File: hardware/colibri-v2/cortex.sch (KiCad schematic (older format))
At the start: 54 parts

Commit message: Work on PWM, USB, MEMS, Power
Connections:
- wire segments 444 -> 363

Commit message: added symbol STM32F429NI
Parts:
- removed R? (x4): 0R, Resistors_SMD:R_0603, symbol R
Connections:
- net labels removed: FMC_A0, FMC_A1, FMC_A10, FMC_A11, FMC_A2, FMC_A3, FMC_A4, FMC_A5, FMC_A6, FMC_A7, FMC_A8, FMC_A9, FMC_A[0..11], FMC_BA0, FMC_BA1, FMC_BA[0..1], FMC_D0, FMC_D1, FMC_D10, FMC_D11, FMC_D12, FMC_D13, FMC_D14, FMC_D15, FMC_D2, FMC_D3, FMC_D4, FMC_D5, FMC_D6, FMC_D7, FMC_D8, FMC_D9, FMC_D[0..15], FMC_NBL0, FMC_NBL1, FMC_NBL[0..1], FMC_SDCKE1, FMC_SDCLK, FMC_SDNCAS, FMC_SDNE1, FMC_SDNRAS, FMC_SDNWE, LCD_A0, LCD_A1, LCD_A2, LCD_A3, LCD_A4, LCD_A5, LCD_B2, LCD_B3, LCD_B4, LCD_B5, LCD_B6, LCD_B7, LCD_CSX, LCD_D0, LCD_D1, LCD_D13, LCD_D14, LCD_D15, LCD_D2, LCD_D3, LCD_DCX_SCL, LCD_DOTCLK, LCD_ENABLE, LCD_G2, LCD_G3, LCD_G4, LCD_G5, LCD_G6, LCD_G7, LCD_HSYNC, LCD_IM0, LCD_IM1, LCD_IM2, LCD_IM3, LCD_R2, LCD_R3, LCD_R4, LCD_R5, LCD_R6, LCD_R7, LCD_RDX, LCD_SDA, LCD_TE, LCD_VSYNC, LCD_WRX_DCX, TP_ACP_RST, TP_I2C3_SCL, TP_I2C3_SDA, TP_INT1
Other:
- moved on the sheet: R?

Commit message: Replaced the cortex processor with STM32F429NI
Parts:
- removed C?: 1u/25V/X7R, Capacitors_SMD:C_0603, symbol C_SMT
- removed R?: 0R/1%, Resistors_SMD:R_0805, symbol R_SMT
- removed U? (x12): STM32F429BI, symbol STM32F429BI
- added C? (x3): 100nF/50V/X7R, Capacitors_SMD:C_0603, symbol C_SMT
- added R?: 0R/1%, Resistors_SMD:R_0805, symbol R_SMT
- added U? (x12): STM32F429NI, symbol STM32F429NI
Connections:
- wire segments 363 -> 381
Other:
- moved on the sheet: C?, FB?, R?, Y?

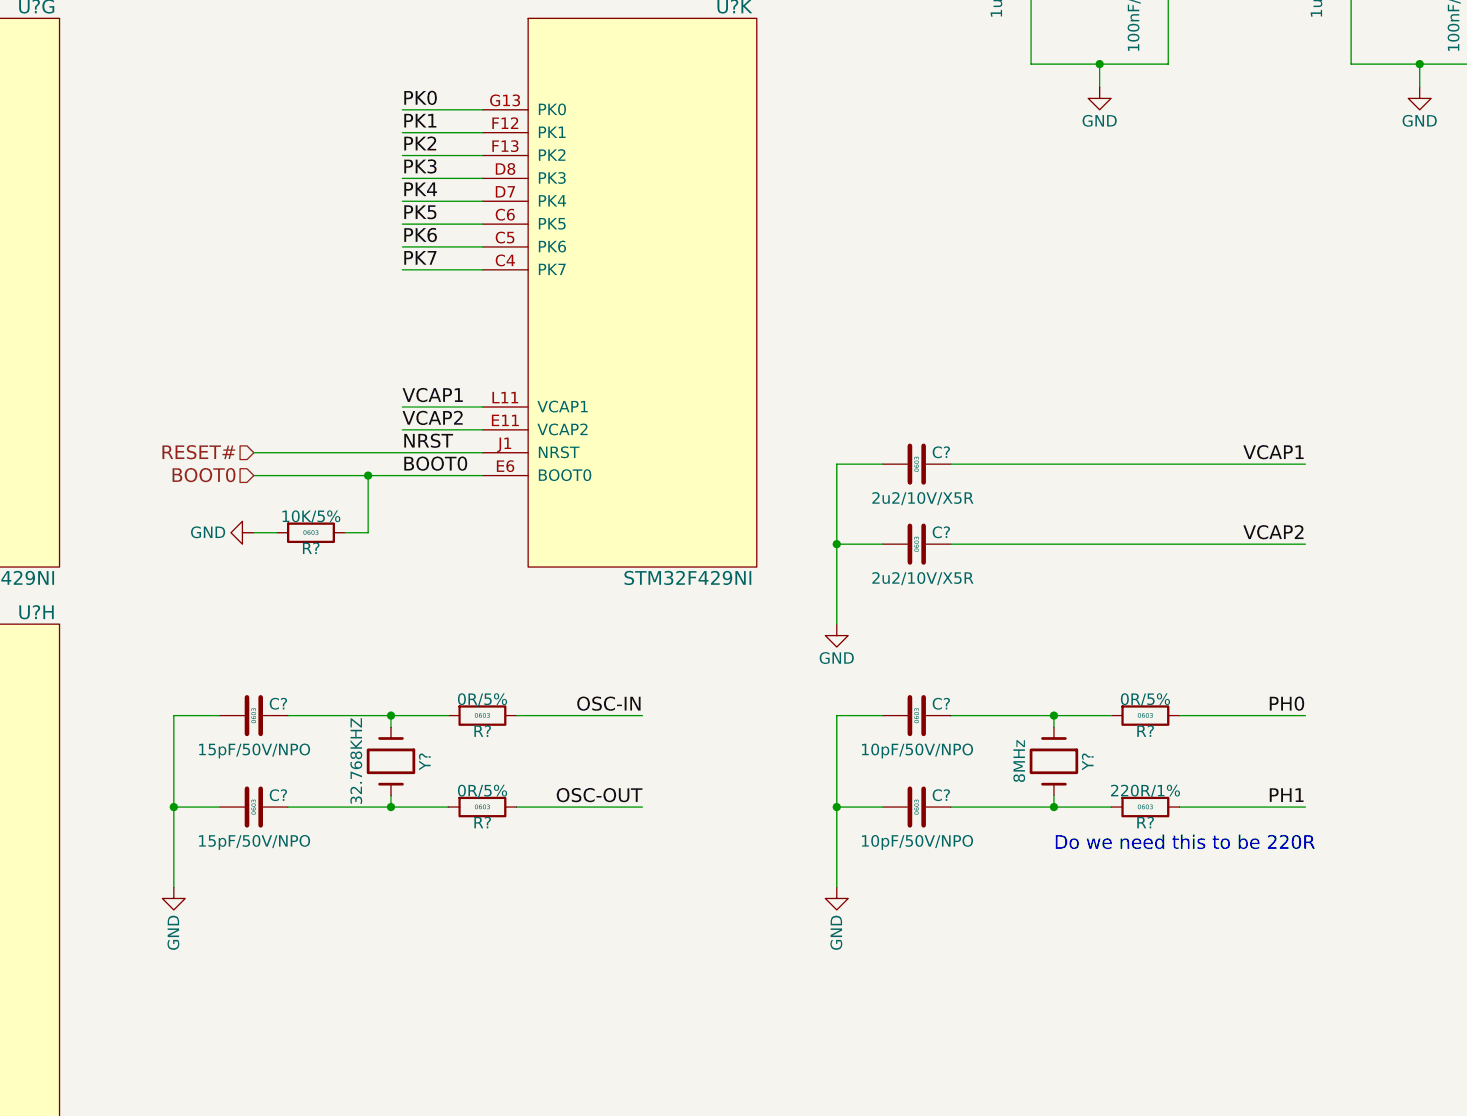
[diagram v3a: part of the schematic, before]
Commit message: Added Power-On-Reset controller MCP120 to the Cortex
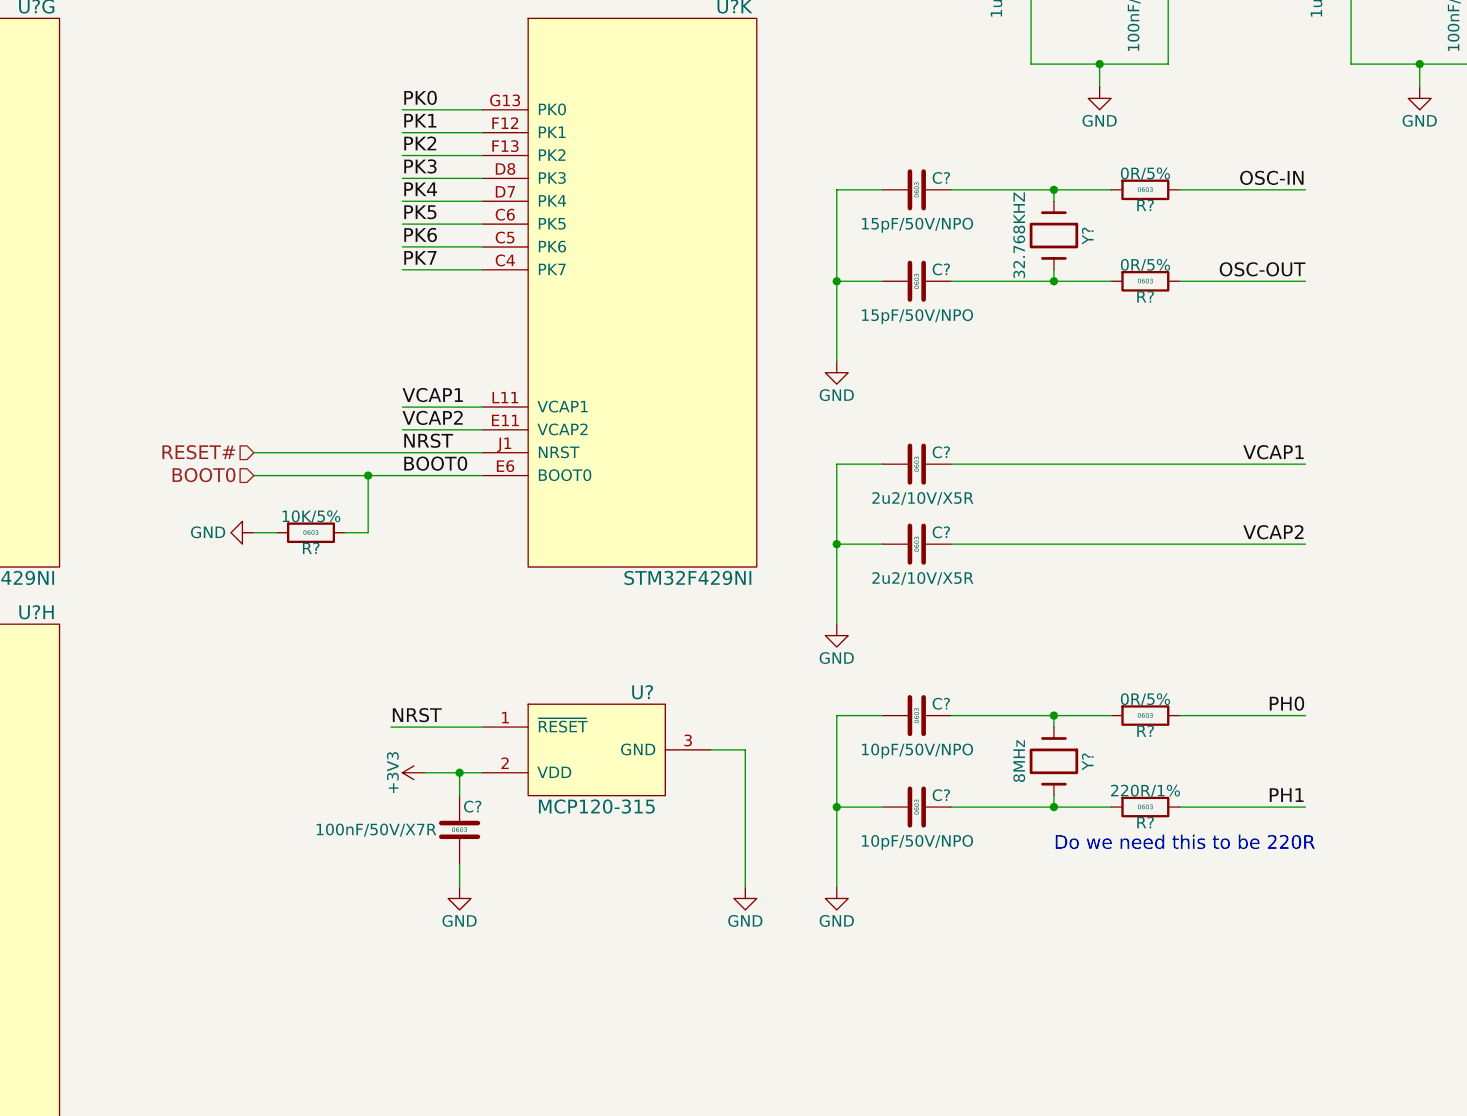
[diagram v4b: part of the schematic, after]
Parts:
- added C?: 100nF/50V/X7R, Capacitors_SMD:C_0603, symbol C_SMT
- added U?: MCP120-315, TO_SOT_Packages_SMD:SOT-23, symbol MCP120/130
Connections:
- net +3V3: now also C?.2, U?.2 (VDD)
- net GND: now also C?.1, U?.3 (GND)
- net RESET#: now also U?.1 (~RESET)
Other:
- moved on the sheet: C?, R?, Y?
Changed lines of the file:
@@
 	0    1    1    0
-$EndComp
-$Comp
-L GND #PWR?
-U 1 1 557D1DFA
-P 10200 9750
-F 0 "#PWR?" H 10200 9500 50  0001 C CNN
-F 1 "GND" V 10200 9550 50  0000 C CNN
-F 2 "" H 10200 9750 60  0000 C CNN
-F 3 "" H 10200 9750 60  0000 C CNN
-	1    10200 9750
-	1    0    0    -1
 $EndComp
 Text Label 2100 1050 0    60   ~ 0
@@
 L Crystal Y?
 U 1 1 5636A5D1
-P 8250 9200
-F 0 "Y?" H 8250 9350 50  0000 C CNN
-F 1 "32.768KHZ" H 8250 9050 50  0000 C CNN
-F 2 "" H 8250 9200 60  0001 C CNN
-F 3 "" H 8250 9200 60  0000 C CNN
-F 4 "3.2mm X 1.5mm" H 8250 9200 30  0001 C CNN "SMT"
-F 5 "2101347" H 8250 9200 60  0001 C CNN "Part"
-F 6 "Farnell" H 8250 9200 60  0001 C CNN "Provider"
-	1    8250 9200
+P 11150 6900
+F 0 "Y?" H 11150 7050 50  0000 C CNN
+F 1 "32.768KHZ" H 11150 6750 50  0000 C CNN
+F 2 "" H 11150 6900 60  0001 C CNN
+F 3 "" H 11150 6900 60  0000 C CNN
+F 4 "3.2mm X 1.5mm" H 11150 6900 30  0001 C CNN "SMT"
+F 5 "2101347" H 11150 6900 60  0001 C CNN "Part"
+F 6 "Farnell" H 11150 6900 60  0001 C CNN "Provider"
+	1    11150 6900
 	0    1    1    0
 $EndComp
-$Comp
-L GND #PWR?
-U 1 1 5636A5D7
-P 7300 9750
-F 0 "#PWR?" H 7300 9500 50  0001 C CNN
-F 1 "GND" V 7300 9550 50  0000 C CNN
-F 2 "" H 7300 9750 60  0000 C CNN
-F 3 "" H 7300 9750 60  0000 C CNN
-	1    7300 9750
-	1    0    0    -1
-$EndComp
-Text Label 9350 9000 2    60   ~ 0
+Text Label 12250 6700 2    60   ~ 0
 OSC-IN
 $Comp
 L C_SMT C?
 U 1 1 5636A5F1
-P 7650 9000
-F 0 "C?" V 7700 8850 50  0000 L CNN
-F 1 "15pF/50V/NPO" V 7500 8750 50  0000 L CNN
-F 2 "Capacitors_SMD:C_0603" H 7680 8850 30  0001 L CNN
-F 3 "" H 7675 9100 60  0000 L CNN
-F 4 "0603" H 7650 9000 20  0000 C CNN "SMT"
-F 5 "1856143" H 7680 8810 30  0001 L CNN "Part"
-F 6 "Farnell" H 7680 8770 30  0001 L CNN "Provider"
-	1    7650 9000
+P 10550 6700
+F 0 "C?" V 10600 6550 50  0000 L CNN
+F 1 "15pF/50V/NPO" V 10400 6450 50  0000 L CNN
+F 2 "Capacitors_SMD:C_0603" H 10580 6550 30  0001 L CNN
+F 3 "" H 10575 6800 60  0000 L CNN
+F 4 "0603" H 10550 6700 20  0000 C CNN "SMT"
+F 5 "1856143" H 10580 6510 30  0001 L CNN "Part"
+F 6 "Farnell" H 10580 6470 30  0001 L CNN "Provider"
+	1    10550 6700
 	0    -1   -1   0
 $EndComp
@@
 L R_SMT R?
 U 1 1 5636A603
-P 8650 9000
-F 0 "R?" V 8720 9000 50  0000 C CNN
-F 1 "0R/5%" V 8580 9000 50  0000 C CNN
-F 2 "Resistors_SMD:R_0603" V 8800 9000 30  0001 C CNN
-F 3 "" V 8730 9000 30  0000 C CNN
-F 4 "0603" V 8650 9000 20  0000 C CNN "SMT"
-F 5 "1469739" V 8850 9000 30  0001 C CNN "Part"
-F 6 "Farnell" V 8900 9000 30  0001 C CNN "Provider"
-	1    8650 9000
+P 11550 6700
+F 0 "R?" V 11620 6700 50  0000 C CNN
+F 1 "0R/5%" V 11480 6700 50  0000 C CNN
+F 2 "Resistors_SMD:R_0603" V 11700 6700 30  0001 C CNN
+F 3 "" V 11630 6700 30  0000 C CNN
+F 4 "0603" V 11550 6700 20  0000 C CNN "SMT"
+F 5 "1469739" V 11750 6700 30  0001 C CNN "Part"
+F 6 "Farnell" V 11800 6700 30  0001 C CNN "Provider"
+	1    11550 6700
 	0    1    1    0
 $EndComp
-Text Label 9350 9400 2    60   ~ 0
+Text Label 12250 7100 2    60   ~ 0
 OSC-OUT
 Text Label 1350 7750 0    60   ~ 0
@@
 L R_SMT R?
 U 1 1 5636CBD7
-P 8650 9400
-F 0 "R?" V 8720 9400 50  0000 C CNN
-F 1 "0R/5%" V 8580 9400 50  0000 C CNN
-F 2 "Resistors_SMD:R_0603" V 8800 9400 30  0001 C CNN
-F 3 "" V 8730 9400 30  0000 C CNN
-F 4 "0603" V 8650 9400 20  0000 C CNN "SMT"
-F 5 "1469739" V 8850 9400 30  0001 C CNN "Part"
-F 6 "Farnell" V 8900 9400 30  0001 C CNN "Provider"
-	1    8650 9400
+P 11550 7100
+F 0 "R?" V 11620 7100 50  0000 C CNN
+F 1 "0R/5%" V 11480 7100 50  0000 C CNN
+F 2 "Resistors_SMD:R_0603" V 11700 7100 30  0001 C CNN
+F 3 "" V 11630 7100 30  0000 C CNN
+F 4 "0603" V 11550 7100 20  0000 C CNN "SMT"
+F 5 "1469739" V 11750 7100 30  0001 C CNN "Part"
+F 6 "Farnell" V 11800 7100 30  0001 C CNN "Provider"
+	1    11550 7100
 	0    1    1    0
 $EndComp
@@
 L C_SMT C?
 U 1 1 5636D509
-P 7650 9400
-F 0 "C?" V 7700 9250 50  0000 L CNN
-F 1 "15pF/50V/NPO" V 7500 9150 50  0000 L CNN
-F 2 "Capacitors_SMD:C_0603" H 7680 9250 30  0001 L CNN
-F 3 "" H 7675 9500 60  0000 L CNN
-F 4 "0603" H 7650 9400 20  0000 C CNN "SMT"
-F 5 "1856143" H 7680 9210 30  0001 L CNN "Part"
-F 6 "Farnell" H 7680 9170 30  0001 L CNN "Provider"
-	1    7650 9400
+P 10550 7100
+F 0 "C?" V 10600 6950 50  0000 L CNN
+F 1 "15pF/50V/NPO" V 10400 6850 50  0000 L CNN
+F 2 "Capacitors_SMD:C_0603" H 10580 6950 30  0001 L CNN
+F 3 "" H 10575 7200 60  0000 L CNN
+F 4 "0603" H 10550 7100 20  0000 C CNN "SMT"
+F 5 "1856143" H 10580 6910 30  0001 L CNN "Part"
+F 6 "Farnell" H 10580 6870 30  0001 L CNN "Provider"
+	1    10550 7100
 	0    -1   -1   0
 $EndComp
@@
 Connection ~ 12450 5450
 Wire Wire Line
-	7800 9000 8250 9000
-Wire Wire Line
-	8250 9000 8500 9000
-Wire Wire Line
-	7800 9400 8250 9400
-Wire Wire Line
-	8250 9400 8500 9400
-Wire Wire Line
-	8250 9350 8250 9400
-Connection ~ 8250 9400
-Wire Wire Line
-	8250 9050 8250 9000
-Connection ~ 8250 9000
-Wire Wire Line
-	7300 9000 7500 9000
-Wire Wire Line
-	7300 9400 7500 9400
-Wire Wire Line
-	7300 9000 7300 9400
-Wire Wire Line
-	7300 9400 7300 9750
-Connection ~ 7300 9400
-Wire Wire Line
-	8800 9000 9350 9000
-Wire Wire Line
-	8800 9400 9350 9400
+	10700 6700 11150 6700
+Wire Wire Line
+	11150 6700 11400 6700
+Wire Wire Line
+	10700 7100 11150 7100
+Wire Wire Line
+	11150 7100 11400 7100
+Wire Wire Line
+	11150 7050 11150 7100
+Connection ~ 11150 7100
+Wire Wire Line
+	11150 6750 11150 6700
+Connection ~ 11150 6700
+Wire Wire Line
+	10200 6700 10400 6700
+Wire Wire Line
+	10200 7100 10400 7100
+Wire Wire Line
+	10200 6700 10200 7100
+Wire Wire Line
+	10200 7100 10200 7450
+Connection ~ 10200 7100
+Wire Wire Line
+	11700 6700 12250 6700
+Wire Wire Line
+	11700 7100 12250 7100
 Wire Wire Line
 	5300 1050 5600 1050
@@
 Wire Wire Line
 	15000 1300 15000 800
+$Comp
+L GND #PWR?
+U 1 1 5652DC2F
+P 10200 7450
+F 0 "#PWR?" H 10200 7200 50  0001 C CNN
+F 1 "GND" H 10200 7300 50  0000 C CNN
+F 2 "" H 10200 7450 60  0000 C CNN
+F 3 "" H 10200 7450 60  0000 C CNN
+	1    10200 7450
+	1    0    0    -1
+$EndComp
+$Comp
+L GND #PWR?
+U 1 1 5652DCD6
+P 10200 9750
+F 0 "#PWR?" H 10200 9500 50  0001 C CNN
+F 1 "GND" H 10200 9600 50  0000 C CNN
+F 2 "" H 10200 9750 60  0000 C CNN
+F 3 "" H 10200 9750 60  0000 C CNN
+	1    10200 9750
+	1    0    0    -1
+$EndComp
+$Comp
+L MCP120/130 U?
+U 1 1 5652DFEF
+P 9150 9150
+F 0 "U?" H 9350 9400 60  0000 C CNN
+F 1 "MCP120-315" H 9150 8900 60  0000 C CNN
+F 2 "TO_SOT_Packages_SMD:SOT-23" H 9150 8800 60  0001 C CNN
+F 3 "" H 9000 9200 60  0000 C CNN
+	1    9150 9150
+	1    0    0    -1
+$EndComp
+Text Label 8250 9050 0    60   ~ 0
+NRST
+$Comp
+L +3V3 #PWR?
+U 1 1 5652E4E0
+P 8400 9250
+F 0 "#PWR?" H 8400 9100 50  0001 C CNN
+F 1 "+3V3" H 8400 9390 50  0000 C CNN
+F 2 "" H 8400 9250 60  0000 C CNN
+F 3 "" H 8400 9250 60  0000 C CNN
+	1    8400 9250
+	0    -1   -1   0
+$EndComp
+Wire Wire Line
+	8400 9250 8550 9250
+Wire Wire Line
+	8550 9250 8650 9250
+Wire Wire Line
+	8250 9050 8650 9050
+$Comp
+L GND #PWR?
+U 1 1 5652ED80
+P 9800 9750
+F 0 "#PWR?" H 9800 9500 50  0001 C CNN
+F 1 "GND" H 9800 9600 50  0000 C CNN
+F 2 "" H 9800 9750 60  0000 C CNN
+F 3 "" H 9800 9750 60  0000 C CNN
+	1    9800 9750
+	1    0    0    -1
+$EndComp
+Wire Wire Line
+	9650 9150 9800 9150
+Wire Wire Line
+	9800 9150 9800 9750
+$Comp
+L C_SMT C?
+U 1 1 5652FAEC
+P 8550 9500
+F 0 "C?" H 8450 9400 50  0000 L CNN
+F 1 "100nF/50V/X7R" H 8650 9500 50  0000 L CNN
+F 2 "Capacitors_SMD:C_0603" H 8580 9350 30  0001 L CNN
+F 3 "" H 8575 9600 60  0000 L CNN
+F 4 "0603" H 8550 9500 20  0000 C CNN "SMT"
+F 5 "1414028" H 8580 9310 30  0001 L CNN "Part"
+F 6 "Farnell" H 8580 9270 30  0001 L CNN "Provider"
+	1    8550 9500
+	-1   0    0    1
+$EndComp
+$Comp
+L GND #PWR?
+U 1 1 565300A3
+P 8550 9750
+F 0 "#PWR?" H 8550 9500 50  0001 C CNN
+F 1 "GND" H 8550 9600 50  0000 C CNN
+F 2 "" H 8550 9750 60  0000 C CNN
+F 3 "" H 8550 9750 60  0000 C CNN
+	1    8550 9750
+	1    0    0    -1
+$EndComp
+Wire Wire Line
+	8550 9350 8550 9250
+Connection ~ 8550 9250
+Wire Wire Line
+	8550 9650 8550 9750
 $EndSCHEMATC

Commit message: Work on Cortex wiring
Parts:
- R?: value 10K/5% -> 10K/5%[NA]
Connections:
- net PA10 renamed USART1_RX
- net PA11 renamed USART1_CTS
- net PA12 renamed USART1_RTS
- net PA9 renamed USART1_TX

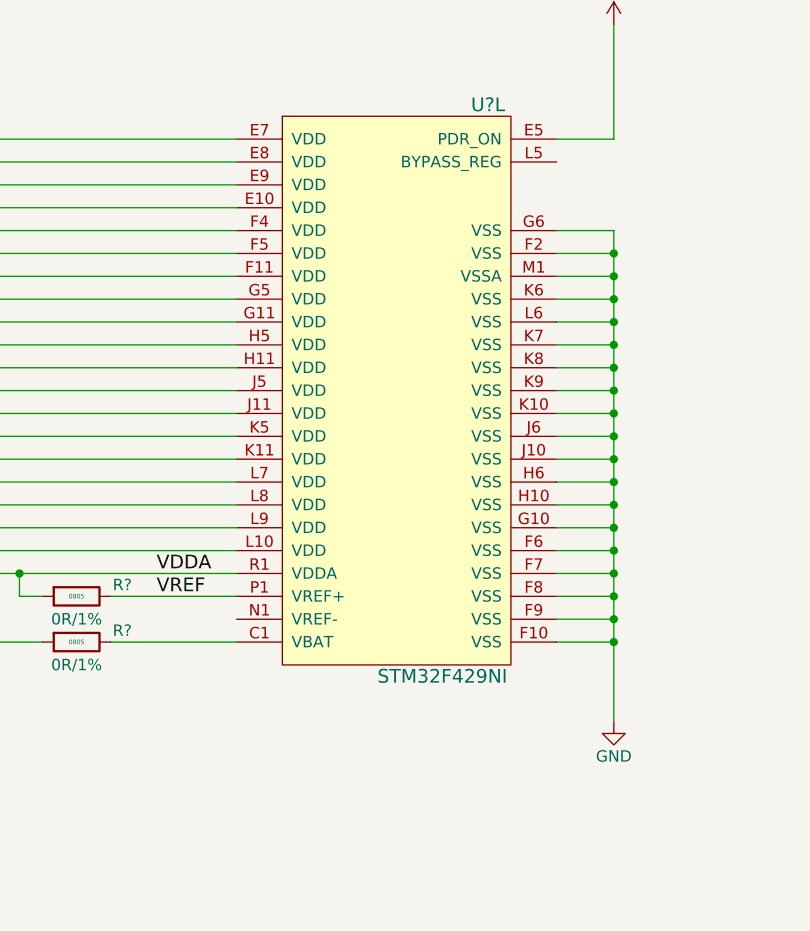
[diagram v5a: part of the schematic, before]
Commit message: Work on power controll, buttons
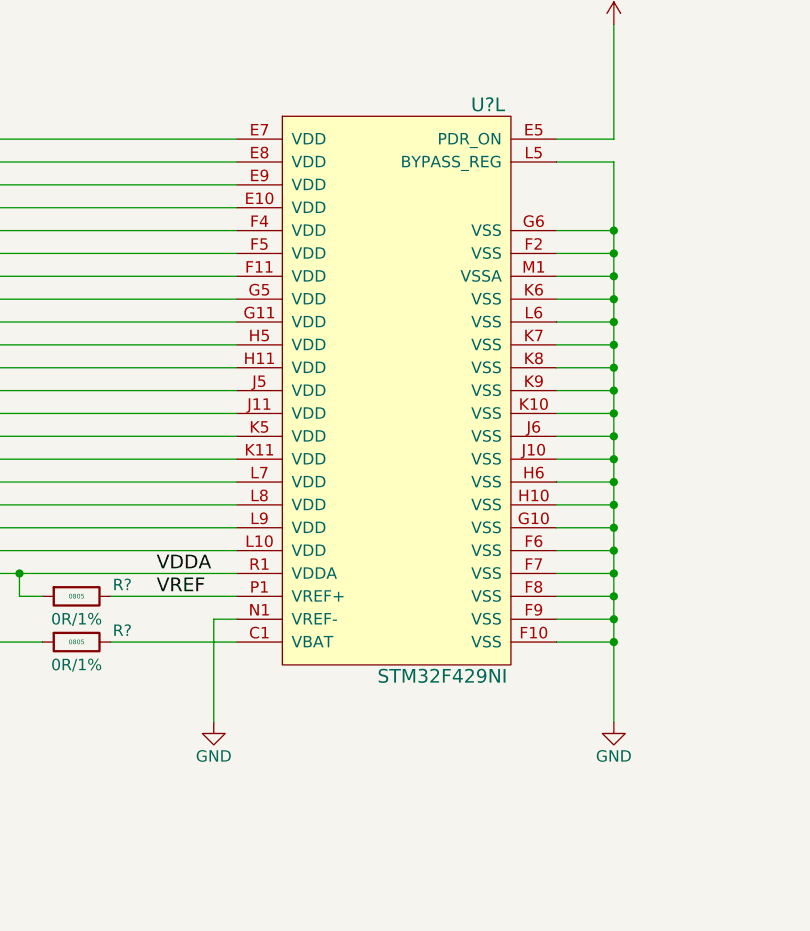
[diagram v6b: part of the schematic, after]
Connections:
- net GND: now also U?.L5 (BYPASS_REG), U?.N1 (VREF-)
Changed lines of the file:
@@
 	11700 800  11700 3500
 Wire Wire Line
-	15000 1700 15000 3850
+	15000 1400 15000 3850
 Wire Wire Line
 	10400 7900 10200 7900
@@
 Text Label 1350 2250 0    60   ~ 0
 USART1_RTS
+Wire Wire Line
+	14750 1400 15000 1400
+Connection ~ 15000 1700
+$Comp
+L GND #PWR?
+U 1 1 56533E69
+P 13250 3850
+F 0 "#PWR?" H 13250 3600 50  0001 C CNN
+F 1 "GND" H 13250 3700 50  0000 C CNN
+F 2 "" H 13250 3850 60  0000 C CNN
+F 3 "" H 13250 3850 60  0000 C CNN
+	1    13250 3850
+	1    0    0    -1
+$EndComp
+Wire Wire Line
+	13350 3400 13250 3400
+Wire Wire Line
+	13250 3400 13250 3850
 $EndSCHEMATC
